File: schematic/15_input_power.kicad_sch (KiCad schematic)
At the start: 16 parts, among them J701 PJ-102AH / 12V DC centre +, Q701 AO3401A, U701 L7805CV

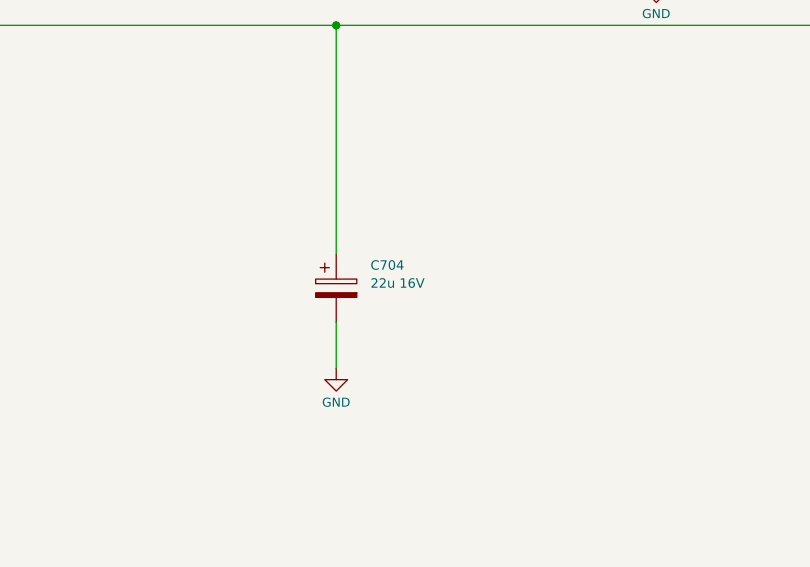
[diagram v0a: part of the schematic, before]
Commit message: pick controls and start pcb placement
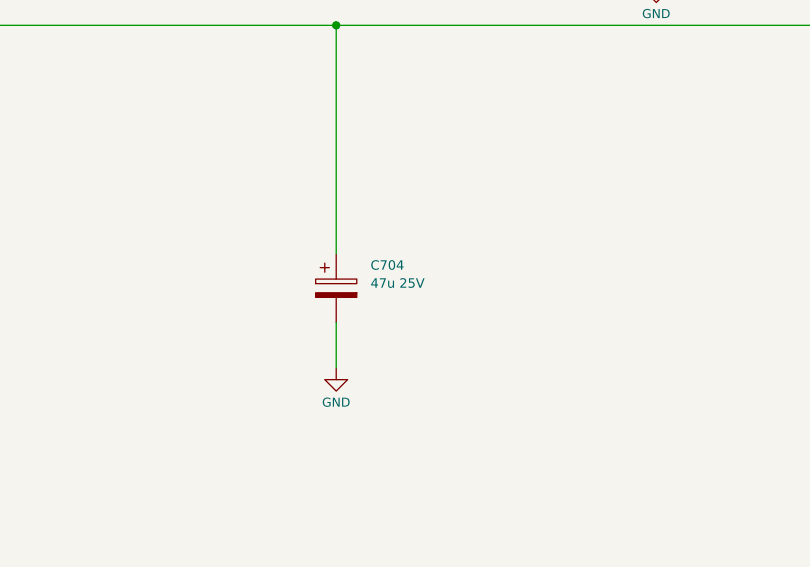
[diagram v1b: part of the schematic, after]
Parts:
- C704: value 22u 16V -> 47u 25V; MPN (none) -> 25YXJ47M5X11; Manufacturer (none) -> Rubycon; Supplier (none) -> DigiKey; Supplier URL (none) -> https://www.digikey.com/en/products/detail/rubycon/25YXJ47M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
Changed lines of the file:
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@@
       )
     )
-    (property "Value" "22u 16V"
+    (property "Value" "47u 25V"
       (at 303.53000000000003 224.25 0.0)
       (effects
@@
         (hide yes)
       )
+    )
+    (property "MPN" "25YXJ47M5X11"
+      (at 299.72 224.79 0.0)
+      (effects
+        (font
+          (size 1.0 1.0)
+        )
+        (hide yes)
+      )
+    )
+    (property "Manufacturer" "Rubycon"
+      (at 299.72 224.79 0.0)
+      (effects
+        (font
+          (size 1.0 1.0)
+        )
+        (hide yes)
+      )
+    )
+    (property "Supplier" "DigiKey"
+      (at 299.72 224.79 0.0)
+      (effects
+        (font
+          (size 1.0 1.0)
+        )
+        (hide yes)
+      )
+    )
+    (property "Supplier URL" "https://www.digikey.com/en/products/detail/rubycon/25YXJ47M5X11/3562900"
+      (at 299.72 224.79 0.0)
+      (effects
+        (font
+          (size 1.0 1.0)
+        )
+        (hide yes)
+      )

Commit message: add the printed case and rear power opening
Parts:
- J701: footprint Connector_BarrelJack:BarrelJack_CUI_PJ-102AH_Horizontal -> Arpeggiator:BarrelJack_PJ102AH_Rear
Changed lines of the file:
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@@
       )
     )
-    (property "Footprint" "Connector_BarrelJack:BarrelJack_CUI_PJ-102AH_Horizontal"
+    (property "Footprint" "Arpeggiator:BarrelJack_PJ102AH_Rear"
       (at 25.4 40.64 0.0)
       (effects

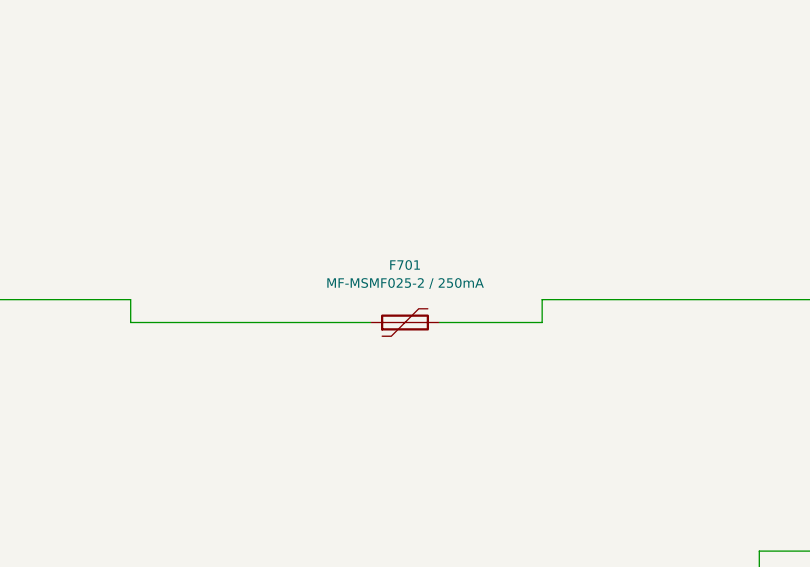
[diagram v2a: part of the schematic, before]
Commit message: parts and cheaper PCB files
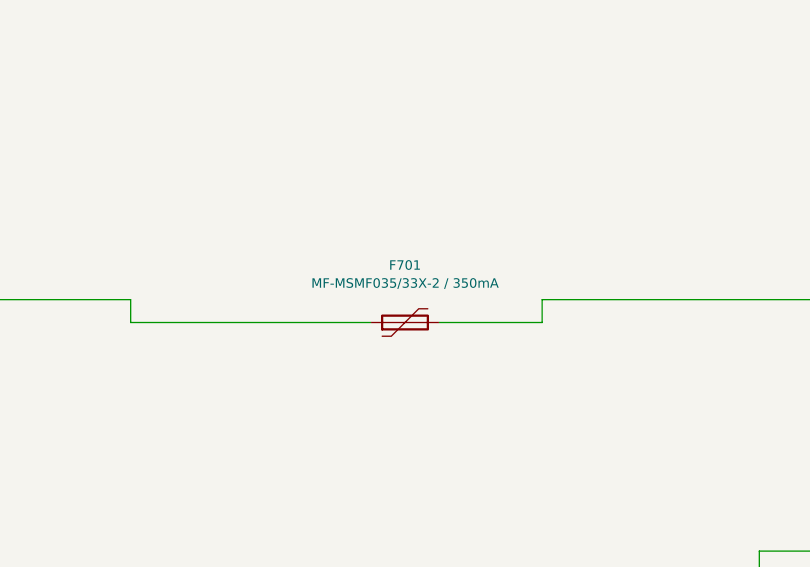
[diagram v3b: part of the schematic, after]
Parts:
- C701: MPN EEU-FR1E101 -> EEU-FC1E101S; Supplier URL https://www.mouser.com/en/ProductDetail/Panasonic-Industry/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 -> https://www.mouser.com/en/ProductDetail/Panasonic/EEU-FC1E1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
- D701: MPN BZT52-C8V2,115 -> BZT52-C8V2J; Supplier LCSC -> Mouser
- D703: MPN SS14-13-F -> SS14-E3/61T; Manufacturer Diodes Incorporated -> Vishay; Supplier LCSC -> Mouser
- F701: value MF-MSMF025-2 / 250mA -> MF-MSMF035/33X-2 / 350mA; MPN MF-MSMF025-2 -> MF-MSMF035/33X-2; Supplier LCSC -> Mouser
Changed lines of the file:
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@@
       )
     )
-    (property "Value" "MF-MSMF025-2 / 250mA"
+    (property "Value" "MF-MSMF035/33X-2 / 350mA"
       (at 110.49 60.419999999999995 90.0)
       (effects
@@
       )
     )
-    (property "Datasheet" "https://www.bourns.com/docs/product-datasheets/mfmsmf.pdf"
+    (property "Datasheet" "https://www.bourns.com/docs/product-datasheets/mf-msmf.pdf"
       (at 110.49 58.419999999999995 90.0)
       (effects
@@
       )
     )
-    (property "MPN" "MF-MSMF025-2"
+    (property "MPN" "MF-MSMF035/33X-2"
       (at 110.49 64.77 0.0)
       (effects
@@
       )
     )
-    (property "Supplier" "LCSC"
+    (property "Supplier" "Mouser"
       (at 110.49 64.77 0.0)
       (effects
@@
       )
     )
-    (property "MPN" "BZT52-C8V2,115"
+    (property "MPN" "BZT52-C8V2J"
       (at 240.03 64.77 0.0)
       (effects
@@
       )
     )
-    (property "Supplier" "LCSC"
+    (property "Supplier" "Mouser"
       (at 240.03 64.77 0.0)
       (effects
@@
       )
     )
-    (property "Datasheet" ""
+    (property "Datasheet" "https://industrial.panasonic.com/cdbs/www-data/pdf/RDF0000/ABA0000C1209.pdf"
       (at 359.41 62.23 0.0)
       (effects
@@
       )
     )
-    (property "MPN" "EEU-FR1E101"
+    (property "MPN" "EEU-FC1E101S"
       (at 355.6 64.77 0.0)
       (effects
@@
       )
     )
-    (property "Supplier URL" "https://www.mouser.com/en/ProductDetail/Panasonic-Industry/EEU-FR1E101?qs=Ao3mORb5HCDieoJwtkb8Dw%3D%3D"
+    (property "Supplier URL" "https://www.mouser.com/en/ProductDetail/Panasonic/EEU-FC1E101S?qs=XZT10BZ%2FaGG7SbPLggsp3w%3D%3D"
       (at 355.6 64.77 0.0)
       (effects
@@
       )
     )
-    (property "Datasheet" "https://www.diodes.com/assets/Datasheets/ds23001.pdf"
+    (property "Datasheet" "https://www.mouser.com/datasheet/2/427/VISH_S_A0010526100_1-2571162.pdf"
       (at 175.26 134.62 0.0)
       (effects
@@
       )
     )
-    (property "MPN" "SS14-13-F"
+    (property "MPN" "SS14-E3/61T"
       (at 175.26 144.78 0.0)
       (effects
@@
       )
     )
-    (property "Manufacturer" "Diodes Incorporated"
+    (property "Manufacturer" "Vishay"
       (at 175.26 144.78 0.0)
       (effects
@@
       )
     )
-    (property "Supplier" "LCSC"
+    (property "Supplier" "Mouser"
       (at 175.26 144.78 0.0)
       (effects
